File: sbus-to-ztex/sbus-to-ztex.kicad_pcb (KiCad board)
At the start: 4 copper layers, 99.7 x 83.8 mm, 45 parts, among them J1 Conn_01x06_Male, J2 47219-2001, J3 Conn_02x07_Odd_Even, J4 USB_B_Micro, J5 Conn_02x06_Odd_Even, U1 SN74CB3T16211DGGR, U2 SN74CB3T16211DGGR, U3 SN74CB3T16211DGGR, U4 SN74CB3T3125PW, U5 SN65220, U7 TPS2065

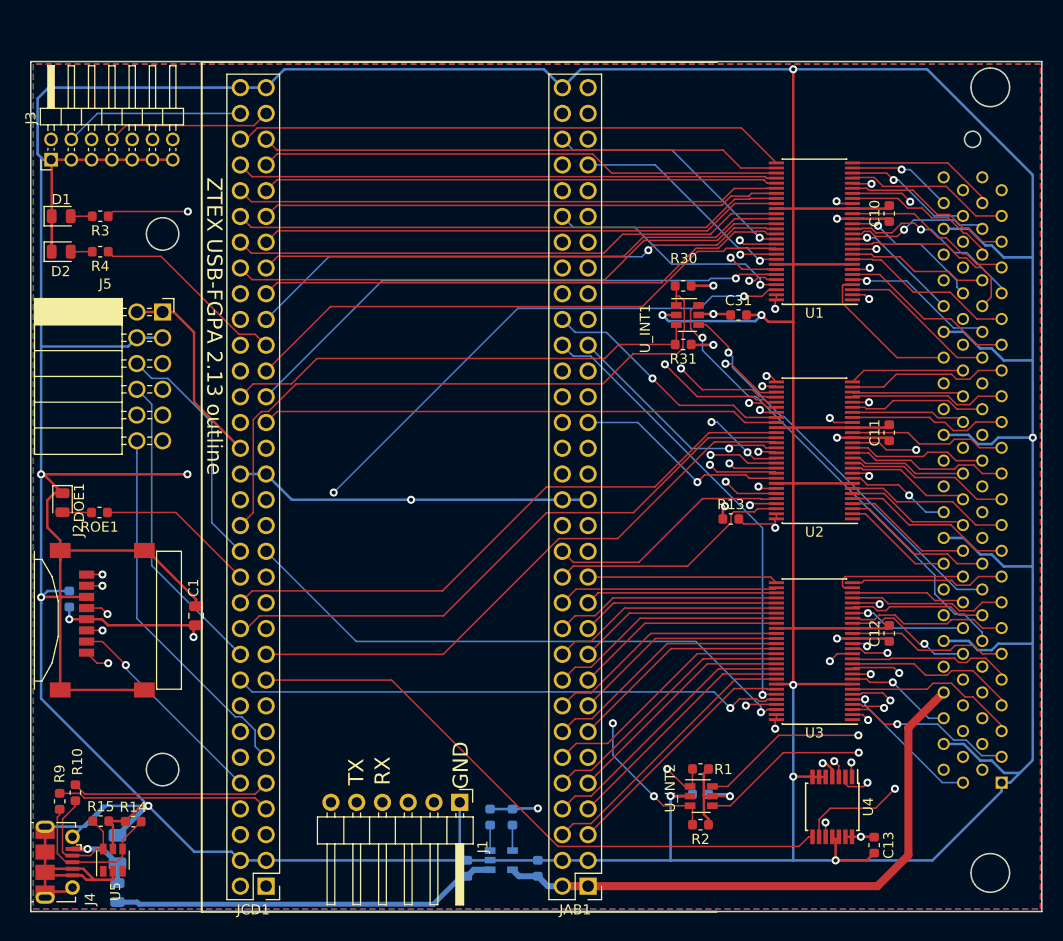
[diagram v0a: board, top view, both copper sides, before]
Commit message: add a pwr header (for e.g. non-pwm fan)
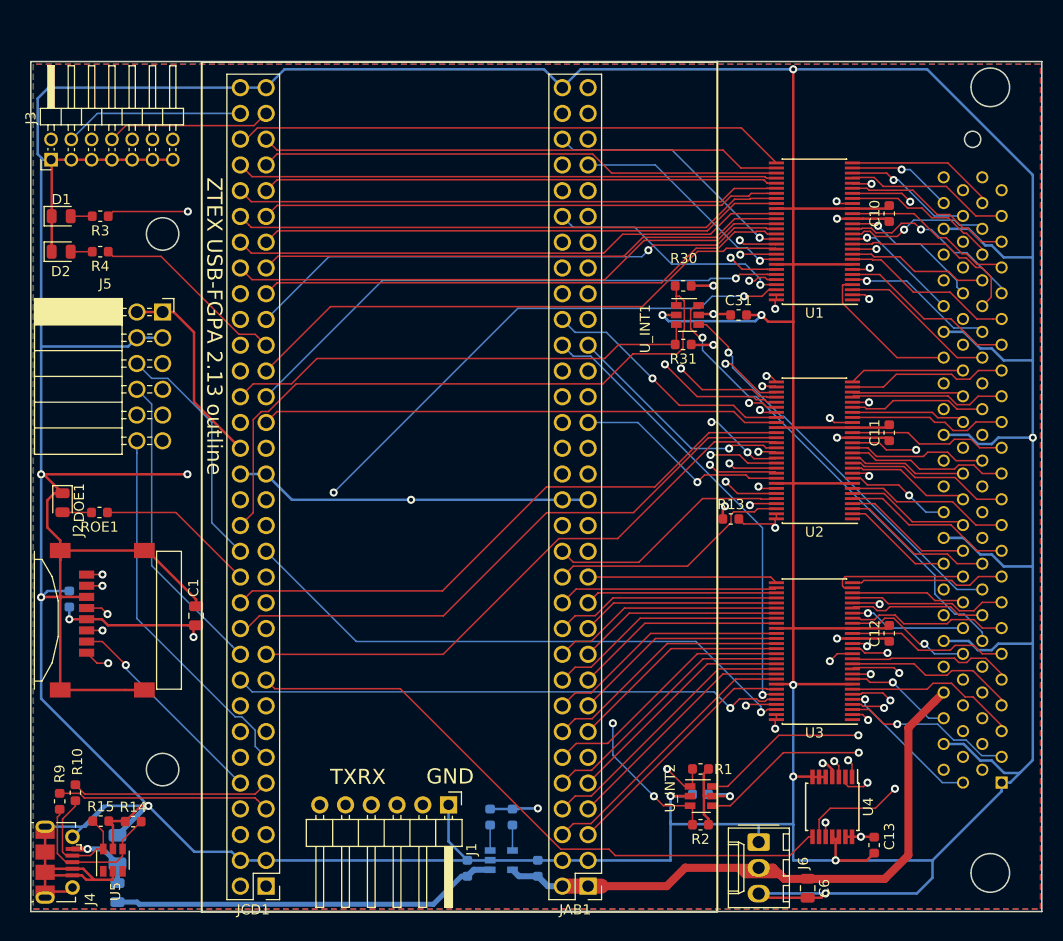
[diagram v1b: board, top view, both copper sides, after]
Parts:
- added C6: 47uF, Capacitor_SMD:C_0805_2012Metric, F.Cu at (173.6, 131.5)
- added J6: Conn_01x03_Male, Connector_Molex:Molex_KK-254_AE-6410-03A_1x03_P2.54mm_Vertical, F.Cu at (168.8, 127.0)
- moved J1 1.13 mm to (138.2, 123.3)
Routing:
- net GND: track 762.6 -> 791.5 mm, vias 13 -> 14
- net +5V: track 103.5 -> 113.2 mm
- net /B2B/TX: track 12.8 -> 11.6 mm
- net /B2B/RX: track 12.8 -> 11.6 mm
- net SBUS_3V3_BG*: track 61.1 -> 61.8 mm

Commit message: more up-to-date
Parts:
- moved R15 2.30 mm to (103.9, 122.6)
- moved C3 2.30 mm to (105.5, 125.4)
- moved R10 2.30 mm to (101.4, 119.8)
- moved R14 2.30 mm to (107.1, 122.7)
- moved R9 2.30 mm to (99.8, 120.7)
- moved U5 2.30 mm to (105.1, 126.5)
- moved FB1 2.30 mm to (105.5, 129.7)
- moved J4 2.30 mm to (99.7, 126.7)
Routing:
- net GND: track 791.5 -> 829.5 mm
- net USBH0_D-: track 19.6 -> 20.6 mm
- net USBH0_D+: track 21.0 -> 21.9 mm
- net /USB/VBus: track 38.2 -> 39.2 mm
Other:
- outline, holes or cut-outs redrawn

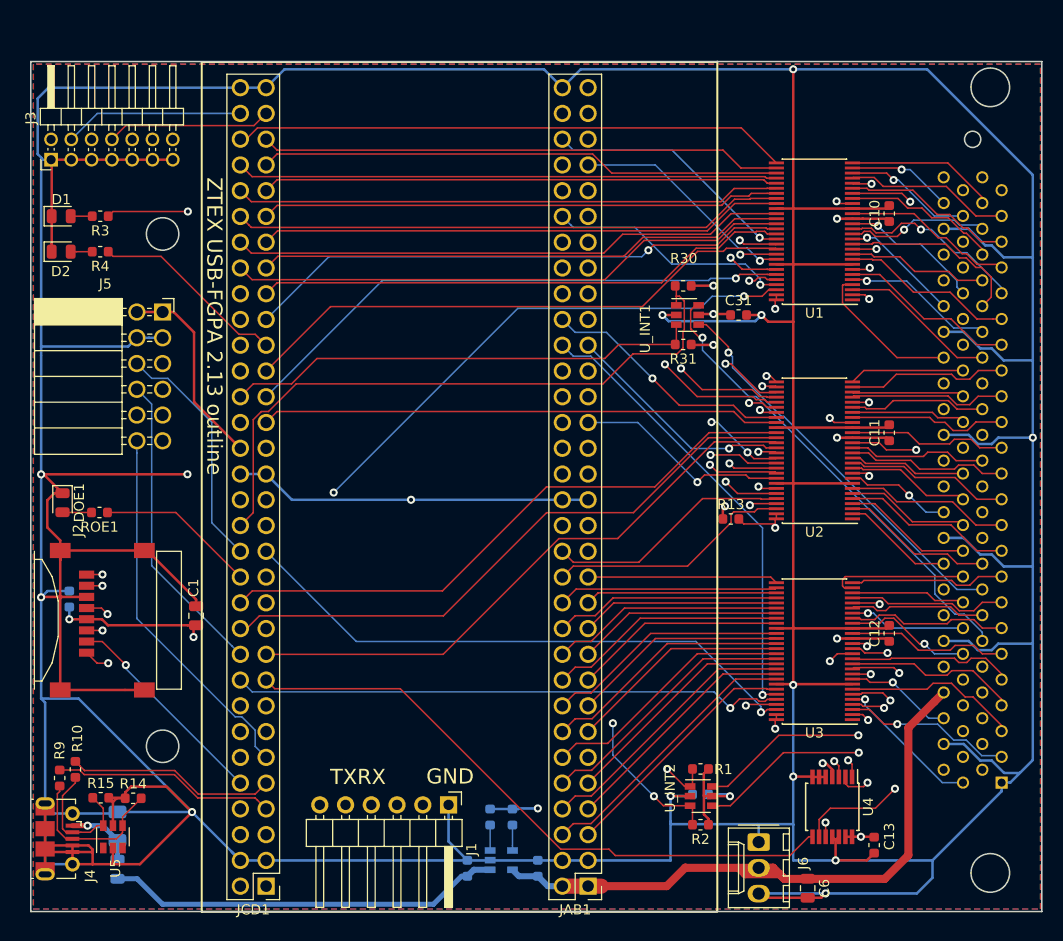
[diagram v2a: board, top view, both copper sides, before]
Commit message: Fewer LEDs, more interrupts, replace USB VBus power chip by something that might be available..., update signals file
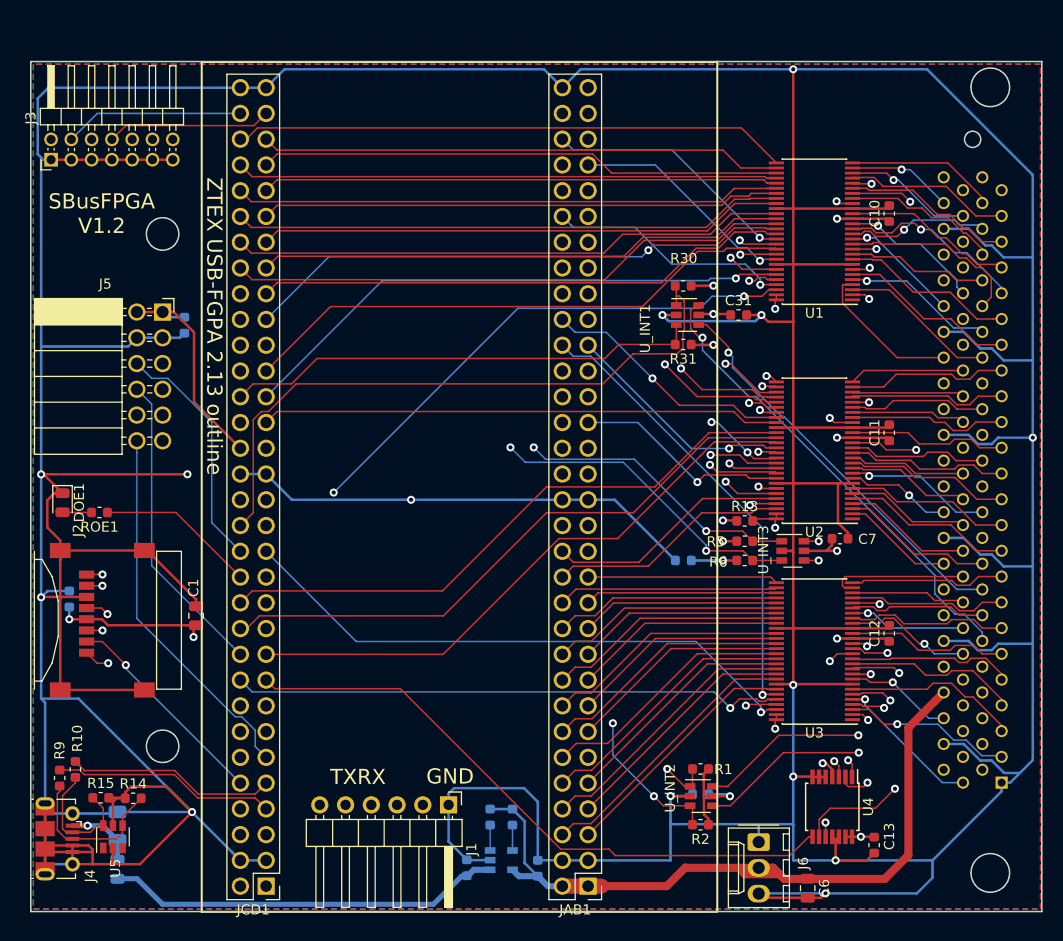
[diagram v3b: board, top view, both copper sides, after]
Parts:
- removed D1, D2: RED, LED_SMD:LED_0805_2012Metric
- removed R20: 1k, Resistor_SMD:R_0603_1608Metric
- removed R3, R4: 549, Resistor_SMD:R_0603_1608Metric
- added C14: 100nF, Capacitor_SMD:C_0603_1608Metric, B.Cu at (140.0, 129.5)
- added C7: 100nF, Capacitor_SMD:C_0603_1608Metric, F.Cu at (176.8, 97.0)
- added C8: 100nF, Capacitor_SMD:C_0603_1608Metric, B.Cu at (161.3, 99.2)
- added C9: 100nF, Capacitor_SMD:C_0603_1608Metric, B.Cu at (112.2, 76.0)
- added R5: 10k, Resistor_SMD:R_0603_1608Metric, F.Cu at (167.4, 97.3)
- added R6: 10k, Resistor_SMD:R_0603_1608Metric, F.Cu at (167.4, 99.2)
- added U_INT3: 74LVC2G07, Package_TO_SOT_SMD:SOT-23-6, F.Cu at (172.2, 98.2)
- C3: value CP -> 150uF
- U7: value TPS2065 -> TPS2051C
- moved R13 1.38 mm to (167.4, 95.3)
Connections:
- J1 pad 2: Net-(J1-Pad2) -> (no net)
- J1 pad 3: Net-(J1-Pad3) -> (no net)
- J1 pad 6: Net-(J1-Pad6) -> (no net)
- J3 pad 12: Net-(J3-Pad12) -> (no net)
- J3 pad 14: Net-(J3-Pad14) -> (no net)
- JAB1 pad 49: LED0 -> SBUS_3V3_INT[6]*
- JCD1 pad 1: Net-(JCD1-Pad1) -> (no net)
- JCD1 pad 2: Net-(JCD1-Pad2) -> (no net)
- JCD1 pad 43: LED1 -> SBUS_3V3_INT[5]*
- R18 pad 2: +3V3 -> +5V
- R19 pad 2: +3V3 -> +5V
- SBus1 pad 28: SBUS_5V_INT[7]* -> (no net)
- SBus1 pad 47: SBUS_5V_DP -> (no net)
- SBus1 pad 48: SBUS_5V_-12V -> (no net)
- SBus1 pad 96: SBUS_5V_+12V -> (no net)
- U1 pad 1: Net-(U1-Pad1) -> (no net)
- U2 pad 1: Net-(U2-Pad1) -> (no net)
- U3 pad 1: Net-(U3-Pad1) -> (no net)
- U5 pad 1: Net-(U5-Pad1) -> (no net)
- U5 pad 3: Net-(U5-Pad3) -> (no net)
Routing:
- net SBUS_3V3_INT[5]*: track 0.00 -> 60.0 mm, vias 0 -> 2
- net SBUS_3V3_INT[6]*: track 0.00 -> 51.6 mm, vias 0 -> 2
- net LED0: track 49.8 -> 0.00 mm, vias 1 -> 0
- net SBUS_5V_INT[6]*: track 0.00 -> 19.8 mm, vias 0 -> 1
- net LED1: track 19.4 -> 0.00 mm
- net SBUS_5V_INT[5]*: track 0.00 -> 18.5 mm, vias 0 -> 1
- net +3V3: track 294.8 -> 283.7 mm, vias 13 -> 15
- net +5V: track 113.2 -> 123.1 mm
- net GND: track 829.5 -> 832.9 mm
- net Net-(D2-Pad2): track 2.12 -> 0.00 mm
- net Net-(D1-Pad2): track 2.12 -> 0.00 mm
- net SBUS_OE: track 121.6 -> 120.2 mm
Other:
- board text added: "SBusFPGA V1.2"

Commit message: Update more stuff to V1.2
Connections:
- J1 pad 2: (no net) -> Net-(J1-Pad2)
- J1 pad 3: (no net) -> Net-(J1-Pad3)
- J1 pad 6: (no net) -> Net-(J1-Pad6)
- J3 pad 12: (no net) -> Net-(J3-Pad12)
- J3 pad 14: (no net) -> Net-(J3-Pad14)
- JAB1 pad 49: SBUS_3V3_INT[6]* -> SBUS_3V3_EER*
- JCD1 pad 1: (no net) -> Net-(JCD1-Pad1)
- JCD1 pad 2: (no net) -> Net-(JCD1-Pad2)
- JCD1 pad 25: SBUS_3V3_EER* -> SBUS_3V3_INT[6]*
- SBus1 pad 28: (no net) -> SBUS_5V_INT[7]*
- SBus1 pad 47: (no net) -> SBUS_5V_DP
- SBus1 pad 48: (no net) -> SBUS_5V_-12V
- SBus1 pad 96: (no net) -> SBUS_5V_+12V
- U1 pad 1: (no net) -> Net-(U1-Pad1)
- U2 pad 1: (no net) -> Net-(U2-Pad1)
- U3 pad 1: (no net) -> Net-(U3-Pad1)
- U5 pad 1: (no net) -> Net-(U5-Pad1)
- U5 pad 3: (no net) -> Net-(U5-Pad3)
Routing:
- net SBUS_3V3_EER*: track 63.0 -> 19.7 mm
- net SBUS_3V3_INT[6]*: track 51.6 -> 53.3 mm, vias 2 -> 1

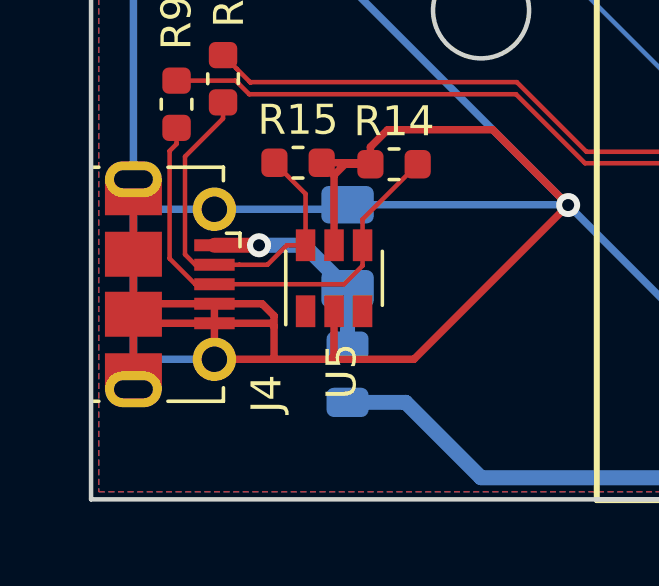
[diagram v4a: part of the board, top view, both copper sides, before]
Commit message: USB ID pin left floating
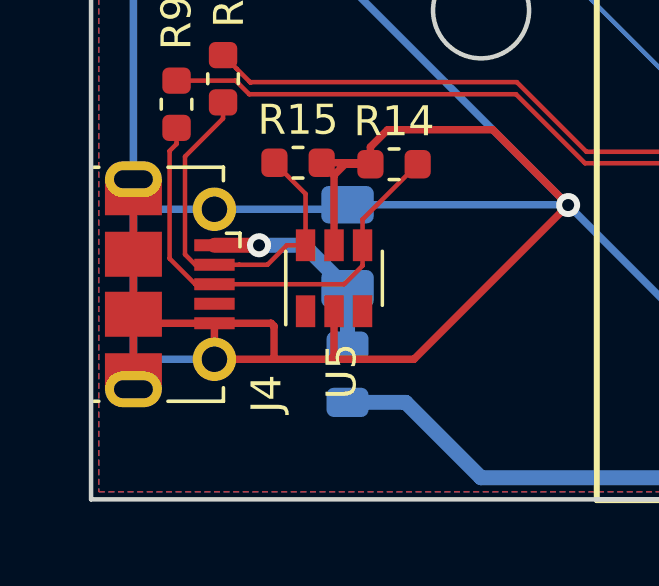
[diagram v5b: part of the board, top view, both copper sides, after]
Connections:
- net Net-(J4-Pad2) renamed /USB/USB_D-
- net Net-(J4-Pad3) renamed /USB/USB_D+
- J1 pad 2: Net-(J1-Pad2) -> (no net)
- J1 pad 3: Net-(J1-Pad3) -> (no net)
- J1 pad 6: Net-(J1-Pad6) -> (no net)
- J3 pad 12: Net-(J3-Pad12) -> (no net)
- J3 pad 14: Net-(J3-Pad14) -> (no net)
- J4 pad 4: GND -> (no net)
- JCD1 pad 1: Net-(JCD1-Pad1) -> (no net)
- JCD1 pad 2: Net-(JCD1-Pad2) -> (no net)
- SBus1 pad 28: SBUS_5V_INT[7]* -> (no net)
- SBus1 pad 47: SBUS_5V_DP -> (no net)
- SBus1 pad 48: SBUS_5V_-12V -> (no net)
- SBus1 pad 96: SBUS_5V_+12V -> (no net)
- U1 pad 1: Net-(U1-Pad1) -> (no net)
- U2 pad 1: Net-(U2-Pad1) -> (no net)
- U3 pad 1: Net-(U3-Pad1) -> (no net)
- U5 pad 1: Net-(U5-Pad1) -> (no net)
- U5 pad 3: Net-(U5-Pad3) -> (no net)
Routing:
- net GND: track 832.9 -> 827.4 mm

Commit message: thinking about a V1.3
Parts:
- removed DOE1: RED, LED_SMD:LED_0805_2012Metric
- removed J1: Conn_01x06_Male, For_SeeedStudio:PinHeader_1x06_P2.54mm_Horizontal_For_SeeedStudio
- removed the J2 at (104.6, 105.1)
- removed J5: Conn_02x06_Odd_Even, For_SeeedStudio:PinSocket_2x06_P2.54mm_Horizontal_For_SeeedStudio
- removed R14, R15: 15k, Resistor_SMD:R_0603_1608Metric
- removed ROE1: 549, Resistor_SMD:R_0603_1608Metric
- removed the U5 at (105.1, 126.5)
- added C15: 100nF 0402, Capacitor_SMD:C_0402_1005Metric, F.Cu at (109.2, 108.0)
- added C16: 10nF 0402, Capacitor_SMD:C_0402_1005Metric, F.Cu at (109.2, 106.5)
- added C17: 47uF 10V 1206, Capacitor_SMD:C_1206_3216Metric, F.Cu at (108.2, 110.5)
- added C18: 100nF 0402, Capacitor_SMD:C_0402_1005Metric, F.Cu at (114.9, 94.5)
- added C19: 100nF 0402, Capacitor_SMD:C_0402_1005Metric, F.Cu at (118.0, 97.3)
- added C20: 100nF 0402, Capacitor_SMD:C_0402_1005Metric, F.Cu at (108.2, 92.0)
- added C21: 10nF 1kV 0805, Capacitor_SMD:C_0805_2012Metric, F.Cu at (100.3, 87.8)
- added C22: 10nF 0402, Capacitor_SMD:C_0402_1005Metric, F.Cu at (134.5, 121.0)
- added C23: 10nF 0402, Capacitor_SMD:C_0402_1005Metric, F.Cu at (164.5, 115.0)
- added C24: 100nF 0402, Capacitor_SMD:C_0402_1005Metric, F.Cu at (149.8, 95.7)
- added C25: 100nF 0402, Capacitor_SMD:C_0402_1005Metric, F.Cu at (109.9, 85.9)
- added C26: 10nF 0402, Capacitor_SMD:C_0402_1005Metric, F.Cu at (112.2, 85.9)
- added C27: 100nF 0402, Capacitor_SMD:C_0402_1005Metric, F.Cu at (172.5, 128.9)
- added H1: MountingHole_Pad, MountingHole:MountingHole_2.2mm_M2_Pad, F.Cu at (100.8, 112.5)
- added J4: 10029449-111RLF (HDMI A), For_SeeedStudio:HDMI_A_Amphenol_10029449-111, F.Cu at (102.2, 99.0)
- added P1: DM3CS-SF, For_SeeedStudio:HRS_DM3CS-SF, F.Cu at (104.5, 75.0)
- added R10: 5.6k, Resistor_SMD:R_0402_1005Metric, F.Cu at (145.5, 121.5)
- added R11: 5.6k, Resistor_SMD:R_0402_1005Metric, F.Cu at (144.0, 119.8)
- added R12: 27, Resistor_SMD:R_0603_1608Metric, F.Cu at (117.5, 83.0)
- added R9: 1M 500V 1206, Resistor_SMD:R_1206_3216Metric, F.Cu at (100.8, 84.8)
- added U10: 74CB3T1G125, Package_TO_SOT_SMD:SOT-23-5, F.Cu at (176.5, 123.5)
- added U6: SRV05-4, Package_TO_SOT_SMD:SOT-23-6, F.Cu at (107.0, 126.3)
- added U7: TPD12S016PWR, For_SeeedStudio:SOP65P640X120-24N, F.Cu at (112.5, 100.7)
- added U8: PCT2075DP, For_SeeedStudio:TSSOP-8_3x3mm_P0.65mm_ForSeeedStudio, F.Cu at (140.0, 120.0)
- added U9: PCT2075DP, For_SeeedStudio:TSSOP-8_3x3mm_P0.65mm_ForSeeedStudio, F.Cu at (165.0, 120.0)
- added X1: ASE-xxxMHz, Oscillator:Oscillator_SMD_Abracon_ASE-4Pin_3.2x2.5mm, F.Cu at (115.6, 86.2)
- C1: value 47uF -> 47uF 10V 1206; footprint Capacitor_SMD:C_0805_2012Metric -> Capacitor_SMD:C_1206_3216Metric
- C10, C11, C12, C13, C31, C7: value 100nF -> 100nF 0402; footprint Capacitor_SMD:C_0603_1608Metric -> Capacitor_SMD:C_0402_1005Metric
- C14, C2, C4, C5, C8: value 100nF -> 100nF 0402; footprint Capacitor_SMD:C_0603_1608Metric -> Capacitor_SMD:C_0402_1005Metric; moved to F.Cu
- C3: value 150uF -> 100uF 1206 (officially 150 uF ? could be >= 100 uF or even less probably); moved to F.Cu
- C6: value 47uF -> 47uF 0805
- C9: value 100nF -> 47uF 0805; footprint Capacitor_SMD:C_0603_1608Metric -> Capacitor_SMD:C_0805_2012Metric; moved to F.Cu
- FB1: moved to F.Cu
- J2: renamed from J4; value USB_B_Micro -> 10118194-0001LF (USB micro-B); footprint Connector_USB:USB_Micro-B_Molex-105017-0001 -> Connector_USB:USB_Micro-B_Amphenol_10118194_Horizontal
- R1, R13, R2, R30, R31, R5, R6: footprint Resistor_SMD:R_0603_1608Metric -> Resistor_SMD:R_0402_1005Metric
- R7: renamed from R18; footprint Resistor_SMD:R_0603_1608Metric -> Resistor_SMD:R_0402_1005Metric; moved to F.Cu
- R8: renamed from R19; footprint Resistor_SMD:R_0603_1608Metric -> Resistor_SMD:R_0402_1005Metric; moved to F.Cu
- U4: value SN74CB3T3125PW -> 74CB3T1G125; footprint Package_SO:TSSOP-14_4.4x5mm_P0.65mm -> Package_TO_SOT_SMD:SOT-23-5
- U5: renamed from U7; value TPS2051C -> TPS2051CDBV; moved to F.Cu
- U_INT1, U_INT2, U_INT3: footprint Package_TO_SOT_SMD:SOT-23-6 -> For_SeeedStudio:SOT65P210X110-6N
- moved J6 76.1 mm to (182.0, 52.0)
- moved C9 67.8 mm to (176.8, 55.5)
- moved C1 40.6 mm to (106.0, 64.8)
- moved C2 37.3 mm to (102.0, 65.8)
- moved C8 34.4 mm to (127.5, 93.2), turned to 0 degrees
- moved J3 33.8 mm to (132.5, 55.2)
- moved FB1 30.5 mm to (136.0, 130.6), turned to 180 degrees
- moved R13 28.1 mm to (179.2, 120.8), turned to 180 degrees
- moved U_INT1 27.3 mm to (176.5, 98.0)
- moved R30 27.3 mm to (173.5, 96.5), turned to 270 degrees
- moved C31 26.8 mm to (180.5, 98.0)
- moved R31 24.8 mm to (173.5, 99.5), turned to 90 degrees
- moved R5 21.6 mm to (173.5, 76.5), turned to 270 degrees
- moved U_INT3 20.7 mm to (176.5, 78.0)
- moved R6 20.7 mm to (173.5, 79.5), turned to 90 degrees
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- renumbered R9 to R3, R10 to R4
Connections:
- C9 pad 1: +3V3 -> +5V
- J2 pad 6: GND -> SHIELD
- JAB1 pad 10: SBUS_3V3_D[04] -> SBUS_OE
- JAB1 pad 11: SBUS_3V3_INT[2]* -> SBUS_3V3_AS*
- JAB1 pad 12: SBUS_3V3_D[06] -> SBUS_3V3_SEL*
- JAB1 pad 13: SBUS_3V3_D[07] -> SBUS_3V3_D[01]
- JAB1 pad 14: SBUS_3V3_D[08] -> SBUS_3V3_D[02]
- JAB1 pad 15: SBUS_3V3_D[09] -> SBUS_3V3_D[04]
- JAB1 pad 16: SBUS_3V3_D[10] -> SBUS_3V3_D[05]
- JAB1 pad 17: SBUS_3V3_D[11] -> SBUS_3V3_D[07]
- JAB1 pad 18: SBUS_3V3_D[12] -> SBUS_3V3_D[08]
- JAB1 pad 19: SBUS_3V3_D[13] -> SBUS_3V3_D[10]
- JAB1 pad 20: SBUS_3V3_D[14] -> SBUS_3V3_CLK
- JAB1 pad 21: SBUS_3V3_D[15] -> SBUS_3V3_D[12]
- JAB1 pad 22: SBUS_3V3_D[16] -> SBUS_3V3_D[13]
- JAB1 pad 23: SBUS_3V3_D[17] -> SBUS_3V3_D[15]
- JAB1 pad 24: SBUS_3V3_D[18] -> SBUS_3V3_D[16]
- JAB1 pad 25: SBUS_3V3_D[19] -> SBUS_3V3_D[18]
- JAB1 pad 26: SBUS_3V3_D[20] -> SBUS_3V3_D[19]
- JAB1 pad 35: SBUS_3V3_D[23] -> SBUS_3V3_D[30]
- JAB1 pad 36: SBUS_3V3_D[24] -> SBUS_3V3_D[31]
- JAB1 pad 37: SBUS_3V3_D[25] -> SBUS_3V3_SIZ[0]
- JAB1 pad 38: SBUS_3V3_D[26] -> SBUS_3V3_PPRD
- JAB1 pad 39: SBUS_3V3_D[27] -> SBUS_3V3_PA[01]
- JAB1 pad 40: SBUS_3V3_D[28] -> SBUS_3V3_PA[00]
- JAB1 pad 41: SBUS_3V3_D[29] -> SBUS_3V3_PA[02]
- JAB1 pad 42: SBUS_3V3_D[30] -> SBUS_3V3_PA[05]
- JAB1 pad 43: SBUS_3V3_D[31] -> SBUS_3V3_EER*
- JAB1 pad 44: SBUS_3V3_CLK -> SBUS_3V3_PA[07]
- JAB1 pad 45: SBUS_3V3_PA[01] -> SBUS_3V3_PA[09]
- JAB1 pad 46: SBUS_3V3_PA[00] -> SBUS_3V3_PA[08]
- JAB1 pad 47: SBUS_3V3_PA[03] -> SBUS_3V3_PA[10]
- JAB1 pad 48: SBUS_3V3_PA[02] -> SBUS_3V3_ACK[0]*
- JAB1 pad 49: SBUS_3V3_EER* -> SBUS_3V3_PA[12]
- JAB1 pad 5: SBUS_3V3_D[01] -> SBUS_3V3_BR*
- JAB1 pad 50: SBUS_3V3_PA[04] -> SBUS_3V3_PA[15]
- JAB1 pad 51: SBUS_3V3_PA[05] -> SBUS_3V3_PA[17]
- JAB1 pad 52: SBUS_3V3_PA[06] -> SBUS_3V3_PA[16]
- JAB1 pad 53: SBUS_3V3_PA[07] -> SBUS_3V3_PA[19]
- JAB1 pad 54: SBUS_3V3_PA[08] -> SBUS_3V3_PA[18]
- JAB1 pad 55: SBUS_3V3_PA[09] -> SBUS_3V3_PA[20]
- JAB1 pad 56: SBUS_3V3_PA[10] -> SBUS_3V3_PA[23]
- JAB1 pad 57: SBUS_3V3_PA[11] -> SBUS_3V3_ACK[2]*
- JAB1 pad 58: SBUS_3V3_PA[12] -> SBUS_3V3_PA[25]
- JAB1 pad 59: SBUS_3V3_PA[13] -> SBUS_3V3_PA[27]
- JAB1 pad 6: SBUS_3V3_D[00] -> I2C0_SDA
- JAB1 pad 60: SBUS_3V3_PA[14] -> SBUS_3V3_PA[26]
- JAB1 pad 7: SBUS_3V3_D[03] -> SBUS_3V3_BG*
- JAB1 pad 8: SBUS_3V3_D[02] -> I2C0_SCL
- JAB1 pad 9: SBUS_3V3_D[05] -> SBUS_3V3_INT[1]*
- JCD1 pad 10: SD_D3 -> HDMI_D2-
- JCD1 pad 11: PMOD-12 -> SBUS_3V3_INT[4]*
- JCD1 pad 12: SD_D0 -> HDMI_D1+
- JCD1 pad 13: PMOD-11 -> SBUS_3V3_INT[5]*
- JCD1 pad 14: SD_D1 -> HDMI_D1-
- JCD1 pad 15: SD_CLK -> SBUS_3V3_INT[6]*
- JCD1 pad 16: SD_CMD -> HDMI_D0+
- JCD1 pad 17: SBUS_3V3_BG* -> SBUS_3V3_D[00]
- JCD1 pad 18: SBUS_3V3_AS* -> HDMI_D0-
- JCD1 pad 19: SBUS_3V3_SIZ[0] -> SBUS_3V3_D[03]
- JCD1 pad 20: PMOD-8 -> HDMI_CLK+
- JCD1 pad 21: SBUS_3V3_BR* -> SBUS_3V3_D[06]
- JCD1 pad 22: SBUS_3V3_SIZ[1] -> HDMI_CLK-
- JCD1 pad 23: SBUS_3V3_INT[1]* -> SBUS_3V3_D[09]
- JCD1 pad 24: SBUS_3V3_SIZ[2] -> SBUS_3V3_D[11]
- JCD1 pad 25: SBUS_3V3_INT[6]* -> SBUS_3V3_D[14]
- JCD1 pad 26: SBUS_DATA_OE_LED -> SBUS_3V3_D[17]
- JCD1 pad 27: SBUS_3V3_RST* -> SBUS_3V3_D[20]
- JCD1 pad 28: PMOD-6 -> SBUS_3V3_D[23]
- JCD1 pad 29: SBUS_3V3_SEL* -> SBUS_3V3_D[24]
- JCD1 pad 30: SBUS_3V3_INT[3]* -> SBUS_3V3_D[25]
- JCD1 pad 37: SBUS_3V3_PPRD -> SBUS_3V3_D[27]
- JCD1 pad 38: SBUS_OE -> SBUS_3V3_D[26]
- JCD1 pad 39: SBUS_3V3_ACK[0]* -> SBUS_3V3_D[28]
- JCD1 pad 40: SBUS_3V3_INT[4]* -> CLK_54_000
- JCD1 pad 41: SBUS_3V3_ACK[1]* -> SBUS_3V3_D[29]
- JCD1 pad 42: PMOD-10 -> SD_D2
- JCD1 pad 43: SBUS_3V3_INT[5]* -> SBUS_3V3_SIZ[1]
- JCD1 pad 44: PMOD-9 -> SD_D3
- JCD1 pad 45: SBUS_3V3_ACK[2]* -> SBUS_3V3_SIZ[2]
- JCD1 pad 46: PMOD-7 -> SD_CMD
- JCD1 pad 47: SBUS_3V3_PA[15] -> SBUS_3V3_PA[03]
- JCD1 pad 48: PMOD-5 -> SD_CLK
- JCD1 pad 49: SBUS_3V3_PA[17] -> SBUS_3V3_PA[04]
- JCD1 pad 5: /B2B/RX -> USBH0_D+
- JCD1 pad 50: SBUS_3V3_PA[16] -> SD_D0
- JCD1 pad 51: SBUS_3V3_PA[19] -> SBUS_3V3_PA[06]
- JCD1 pad 52: SBUS_3V3_PA[18] -> SD_D1
- JCD1 pad 53: SBUS_3V3_PA[21] -> SBUS_3V3_PA[11]
- JCD1 pad 54: SBUS_3V3_PA[20] -> SBUS_3V3_PA[13]
- JCD1 pad 55: SBUS_3V3_PA[23] -> SBUS_3V3_PA[14]
- JCD1 pad 56: SBUS_3V3_PA[22] -> SBUS_3V3_ACK[1]*
- JCD1 pad 57: SBUS_3V3_PA[25] -> SBUS_3V3_PA[21]
- JCD1 pad 58: SBUS_3V3_PA[24] -> SBUS_3V3_PA[22]
- JCD1 pad 59: SBUS_3V3_PA[27] -> SBUS_3V3_PA[24]
- JCD1 pad 6: /B2B/TX -> USBH0_D-
- JCD1 pad 60: SBUS_3V3_PA[26] -> SBUS_3V3_RST*
- JCD1 pad 7: USBH0_D+ -> SBUS_3V3_INT[2]*
- JCD1 pad 8: SD_D2 -> HDMI_D2+
- JCD1 pad 9: USBH0_D- -> SBUS_3V3_INT[3]*
- R30 pad 2: SBUS_3V3_INT[3]* -> SBUS_3V3_INT[4]*
- R31 pad 2: SBUS_3V3_INT[4]* -> SBUS_3V3_INT[3]*
- U1 pad 10: SBUS_5V_ACK[1]* -> SBUS_3V3_PA[23]
- U1 pad 11: SBUS_5V_PA[13] -> SBUS_3V3_PA[20]
- U1 pad 12: SBUS_5V_PA[14] -> SBUS_3V3_PA[21]
- U1 pad 13: SBUS_5V_PA[15] -> SBUS_3V3_PA[18]
- U1 pad 14: SBUS_5V_ACK[2]* -> SBUS_3V3_PA[19]
- U1 pad 15: SBUS_5V_PA[16] -> SBUS_3V3_ACK[1]*
- U1 pad 16: SBUS_5V_PA[17] -> SBUS_3V3_PA[16]
- U1 pad 18: SBUS_5V_PA[18] -> SBUS_3V3_PA[17]
- U1 pad 2: SBUS_5V_EER* -> SBUS_3V3_RST*
- U1 pad 20: SBUS_5V_PA[19] -> SBUS_3V3_PA[14]
- U1 pad 21: SBUS_5V_PA[20] -> SBUS_3V3_PA[15]
- U1 pad 22: SBUS_5V_PA[21] -> SBUS_3V3_PA[12]
- U1 pad 23: SBUS_5V_PA[22] -> SBUS_3V3_PA[13]
- U1 pad 24: SBUS_5V_PA[23] -> SBUS_3V3_ACK[0]*
- U1 pad 25: SBUS_5V_PA[24] -> SBUS_3V3_PA[10]
- U1 pad 26: SBUS_5V_PA[25] -> SBUS_3V3_PA[11]
- U1 pad 27: SBUS_5V_PA[27] -> SBUS_3V3_PA[08]
- U1 pad 28: SBUS_5V_PA[26] -> SBUS_3V3_PA[09]
- U1 pad 29: SBUS_3V3_PA[26] -> SBUS_5V_PA[09]
- U1 pad 3: SBUS_5V_PA[08] -> SBUS_3V3_PA[26]
- U1 pad 30: SBUS_3V3_PA[27] -> SBUS_5V_PA[08]
- U1 pad 31: SBUS_3V3_PA[25] -> SBUS_5V_PA[11]
- U1 pad 32: SBUS_3V3_PA[24] -> SBUS_5V_PA[10]
- U1 pad 33: SBUS_3V3_PA[23] -> SBUS_5V_ACK[0]*
- U1 pad 34: SBUS_3V3_PA[22] -> SBUS_5V_PA[13]
- U1 pad 35: SBUS_3V3_PA[21] -> SBUS_5V_PA[12]
- U1 pad 36: SBUS_3V3_PA[20] -> SBUS_5V_PA[15]
- U1 pad 37: SBUS_3V3_PA[19] -> SBUS_5V_PA[14]
- U1 pad 39: SBUS_3V3_PA[18] -> SBUS_5V_PA[17]
- U1 pad 4: SBUS_5V_PA[09] -> SBUS_3V3_PA[27]
- U1 pad 40: SBUS_3V3_PA[17] -> SBUS_5V_PA[16]
- U1 pad 41: SBUS_3V3_PA[16] -> SBUS_5V_ACK[1]*
- U1 pad 42: SBUS_3V3_ACK[2]* -> SBUS_5V_PA[19]
- U1 pad 43: SBUS_3V3_PA[15] -> SBUS_5V_PA[18]
- U1 pad 44: SBUS_3V3_PA[14] -> SBUS_5V_PA[21]
- U1 pad 45: SBUS_3V3_PA[13] -> SBUS_5V_PA[20]
- U1 pad 46: SBUS_3V3_ACK[1]* -> SBUS_5V_PA[23]
- U1 pad 47: SBUS_3V3_PA[12] -> SBUS_5V_PA[22]
- U1 pad 48: SBUS_3V3_PA[11] -> SBUS_5V_ACK[2]*
- U1 pad 5: SBUS_5V_ACK[0]* -> SBUS_3V3_PA[24]
- U1 pad 50: SBUS_3V3_PA[10] -> SBUS_5V_PA[25]
- U1 pad 51: SBUS_3V3_ACK[0]* -> SBUS_5V_PA[24]
- U1 pad 52: SBUS_3V3_PA[09] -> SBUS_5V_PA[27]
- U1 pad 53: SBUS_3V3_PA[08] -> SBUS_5V_PA[26]
- U1 pad 54: SBUS_3V3_EER* -> SBUS_5V_RST*
- U1 pad 6: SBUS_5V_PA[10] -> SBUS_3V3_PA[25]
- U1 pad 7: SBUS_5V_PA[11] -> SBUS_3V3_ACK[2]*
- U1 pad 9: SBUS_5V_PA[12] -> SBUS_3V3_PA[22]
- U2 pad 10: SBUS_5V_D[27] -> SBUS_3V3_PA[00]
- U2 pad 11: SBUS_5V_D[28] -> SBUS_3V3_PA[01]
- U2 pad 12: SBUS_5V_D[29] -> SBUS_3V3_SIZ[2]
- U2 pad 13: SBUS_5V_D[30] -> SBUS_3V3_PPRD
- U2 pad 14: SBUS_5V_D[31] -> SBUS_3V3_SIZ[0]
- U2 pad 15: SBUS_5V_SIZ[0] -> SBUS_3V3_SIZ[1]
- U2 pad 16: SBUS_5V_SIZ[1] -> SBUS_3V3_D[31]
- U2 pad 18: SBUS_5V_SIZ[2] -> SBUS_3V3_D[30]
- U2 pad 2: SBUS_5V_D[20] -> SBUS_3V3_PA[06]
- U2 pad 20: SBUS_5V_PPRD -> SBUS_3V3_D[29]
- U2 pad 21: SBUS_5V_PA[00] -> SBUS_3V3_D[28]
- U2 pad 22: SBUS_5V_PA[01] -> SBUS_3V3_D[27]
- U2 pad 23: SBUS_5V_PA[02] -> SBUS_3V3_D[26]
- U2 pad 24: SBUS_5V_PA[03] -> SBUS_3V3_D[25]
- U2 pad 25: SBUS_5V_PA[04] -> SBUS_3V3_D[24]
- U2 pad 26: SBUS_5V_PA[05] -> SBUS_3V3_D[23]
- U2 pad 27: SBUS_5V_PA[06] -> SBUS_3V3_D[22]
- U2 pad 28: SBUS_5V_PA[07] -> SBUS_3V3_D[21]
- U2 pad 29: SBUS_3V3_PA[07] -> SBUS_5V_D[21]
- U2 pad 3: SBUS_5V_D[21] -> SBUS_3V3_PA[07]
- U2 pad 30: SBUS_3V3_PA[06] -> SBUS_5V_D[22]
- U2 pad 31: SBUS_3V3_PA[05] -> SBUS_5V_D[23]
- U2 pad 32: SBUS_3V3_PA[04] -> SBUS_5V_D[24]
- U2 pad 33: SBUS_3V3_PA[03] -> SBUS_5V_D[25]
- U2 pad 34: SBUS_3V3_PA[02] -> SBUS_5V_D[26]
- U2 pad 35: SBUS_3V3_PA[01] -> SBUS_5V_D[27]
- U2 pad 36: SBUS_3V3_PA[00] -> SBUS_5V_D[28]
- U2 pad 37: SBUS_3V3_PPRD -> SBUS_5V_D[29]
- U2 pad 39: SBUS_3V3_SIZ[2] -> SBUS_5V_D[30]
- U2 pad 4: SBUS_5V_D[22] -> SBUS_3V3_EER*
- U2 pad 40: SBUS_3V3_SIZ[1] -> SBUS_5V_D[31]
- U2 pad 41: SBUS_3V3_SIZ[0] -> SBUS_5V_SIZ[1]
- U2 pad 42: SBUS_3V3_D[31] -> SBUS_5V_SIZ[0]
- U2 pad 43: SBUS_3V3_D[30] -> SBUS_5V_PPRD
- U2 pad 44: SBUS_3V3_D[29] -> SBUS_5V_SIZ[2]
- U2 pad 45: SBUS_3V3_D[28] -> SBUS_5V_PA[01]
- U2 pad 46: SBUS_3V3_D[27] -> SBUS_5V_PA[00]
- U2 pad 47: SBUS_3V3_D[26] -> SBUS_5V_PA[03]
- U2 pad 48: SBUS_3V3_D[25] -> SBUS_5V_PA[02]
- U2 pad 5: SBUS_5V_D[23] -> SBUS_3V3_PA[04]
- U2 pad 50: SBUS_3V3_D[24] -> SBUS_5V_PA[05]
- U2 pad 51: SBUS_3V3_D[23] -> SBUS_5V_PA[04]
- U2 pad 52: SBUS_3V3_D[22] -> SBUS_5V_EER*
- U2 pad 53: SBUS_3V3_D[21] -> SBUS_5V_PA[07]
- U2 pad 54: SBUS_3V3_D[20] -> SBUS_5V_PA[06]
- U2 pad 6: SBUS_5V_D[24] -> SBUS_3V3_PA[05]
- U2 pad 7: SBUS_5V_D[25] -> SBUS_3V3_PA[02]
- U2 pad 9: SBUS_5V_D[26] -> SBUS_3V3_PA[03]
- U3 pad 10: SBUS_5V_D[02] -> SBUS_3V3_D[13]
- U3 pad 11: SBUS_5V_D[05] -> SBUS_3V3_D[12]
- U3 pad 12: SBUS_5V_D[04] -> SBUS_3V3_D[11]
- U3 pad 13: SBUS_5V_D[06] -> SBUS_3V3_D[10]
- U3 pad 14: SBUS_5V_D[07] -> SBUS_3V3_D[09]
- U3 pad 15: SBUS_5V_D[08] -> SBUS_3V3_D[08]
- U3 pad 16: SBUS_5V_D[09] -> SBUS_3V3_D[07]
- U3 pad 18: SBUS_5V_D[10] -> SBUS_3V3_D[06]
- U3 pad 2: SBUS_5V_RST* -> SBUS_3V3_D[20]
- U3 pad 20: SBUS_5V_D[11] -> SBUS_3V3_D[05]
- U3 pad 21: SBUS_5V_D[12] -> SBUS_3V3_D[04]
- U3 pad 22: SBUS_5V_D[13] -> SBUS_3V3_D[03]
- U3 pad 23: SBUS_5V_D[14] -> SBUS_3V3_D[02]
- U3 pad 24: SBUS_5V_D[15] -> SBUS_3V3_D[01]
- U3 pad 25: SBUS_5V_D[16] -> SBUS_3V3_D[00]
- U3 pad 26: SBUS_5V_D[17] -> SBUS_3V3_SEL*
- U3 pad 27: SBUS_5V_D[18] -> SBUS_3V3_AS*
- U3 pad 28: SBUS_5V_D[19] -> SBUS_3V3_CLK
- U3 pad 29: SBUS_3V3_D[19] -> SBUS_5V_CLK
- U3 pad 3: SBUS_5V_SEL* -> SBUS_3V3_D[19]
- U3 pad 30: SBUS_3V3_D[18] -> SBUS_5V_AS*
- U3 pad 31: SBUS_3V3_D[17] -> SBUS_5V_SEL*
- U3 pad 32: SBUS_3V3_D[16] -> SBUS_5V_D[00]
- U3 pad 33: SBUS_3V3_D[15] -> SBUS_5V_D[01]
- U3 pad 34: SBUS_3V3_D[14] -> SBUS_5V_D[02]
- U3 pad 35: SBUS_3V3_D[13] -> SBUS_5V_D[03]
- U3 pad 36: SBUS_3V3_D[12] -> SBUS_5V_D[04]
- U3 pad 37: SBUS_3V3_D[11] -> SBUS_5V_D[05]
- U3 pad 39: SBUS_3V3_D[10] -> SBUS_5V_D[06]
- U3 pad 4: SBUS_5V_AS* -> SBUS_3V3_D[18]
- U3 pad 40: SBUS_3V3_D[09] -> SBUS_5V_D[07]
- U3 pad 41: SBUS_3V3_D[08] -> SBUS_5V_D[08]
- U3 pad 42: SBUS_3V3_D[07] -> SBUS_5V_D[09]
- U3 pad 43: SBUS_3V3_D[06] -> SBUS_5V_D[10]
- U3 pad 44: SBUS_3V3_D[04] -> SBUS_5V_D[11]
- U3 pad 45: SBUS_3V3_D[05] -> SBUS_5V_D[12]
- U3 pad 46: SBUS_3V3_D[02] -> SBUS_5V_D[13]
- U3 pad 47: SBUS_3V3_D[03] -> SBUS_5V_D[14]
- U3 pad 48: SBUS_3V3_D[00] -> SBUS_5V_D[15]
- U3 pad 5: SBUS_5V_CLK -> SBUS_3V3_D[17]
- U3 pad 50: SBUS_3V3_D[01] -> SBUS_5V_D[16]
- U3 pad 51: SBUS_3V3_CLK -> SBUS_5V_D[17]
- U3 pad 52: SBUS_3V3_AS* -> SBUS_5V_D[18]
- U3 pad 53: SBUS_3V3_SEL* -> SBUS_5V_D[19]
- U3 pad 54: SBUS_3V3_RST* -> SBUS_5V_D[20]
- U3 pad 6: SBUS_5V_D[01] -> SBUS_3V3_D[16]
- U3 pad 7: SBUS_5V_D[00] -> SBUS_3V3_D[15]
- U3 pad 9: SBUS_5V_D[03] -> SBUS_3V3_D[14]
- U4 pad 3: SBUS_3V3_BR* -> GND
- U4 pad 4: +3V3 -> SBUS_3V3_BR*
- U4 pad 5: GND -> +3V3
- U_INT1 pad 1: SBUS_3V3_INT[3]* -> SBUS_3V3_INT[4]*
- U_INT1 pad 3: SBUS_3V3_INT[4]* -> SBUS_3V3_INT[3]*
- U_INT1 pad 4: SBUS_5V_INT[4]* -> SBUS_5V_INT[3]*
- U_INT1 pad 6: SBUS_5V_INT[3]* -> SBUS_5V_INT[4]*
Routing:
- net GND: track 827.4 -> 105.4 mm, vias 14 -> 52
- net +3V3: track 283.7 -> 80.6 mm, vias 15 -> 25
- net SHIELD: track 0.00 -> 62.2 mm
- net SBUS_5V_RST*: track 57.9 -> 10.4 mm, vias 1 -> 0
- net SBUS_3V3_BR*: track 63.2 -> 20.0 mm, vias 1 -> 0
- net SBUS_3V3_SIZ[0]: track 59.0 -> 16.4 mm
- net SBUS_3V3_INT[2]*: track 13.2 -> 55.2 mm
- net SBUS_3V3_BG*: track 61.8 -> 20.1 mm
- net SBUS_3V3_SEL*: track 57.7 -> 20.0 mm, vias 1 -> 0
- net SBUS_3V3_PA[20]: track 54.5 -> 17.0 mm
- net SBUS_3V3_AS*: track 54.6 -> 17.3 mm, vias 1 -> 0
- net SBUS_3V3_ACK[2]*: track 54.1 -> 17.2 mm, vias 1 -> 0
- net PMOD-12: track 36.9 -> 0.00 mm
- net SBUS_3V3_ACK[0]*: track 55.4 -> 18.9 mm, vias 1 -> 0
- net SBUS_3V3_PA[16]: track 55.6 -> 19.3 mm
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- added copper zone on In2.Cu, net +5V
- added copper zone on In1.Cu, net GND
- removed copper zone on In1.Cu, net +3V3
- removed copper zone on In1.Cu, net /USB/VBus_USB0
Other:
- outline, holes or cut-outs redrawn
- net class Default: via_dia 0.8 -> 0.45; via_drill 0.4 -> 0.3
- board text added: "1"
- board text added: "JTAG"
- board text added: "SBusFPGA V1.3"
- board text added: "ZTex 2.13 outline"
- board text removed: "GND"
- board text removed: "RX"
- board text removed: "SBusFPGA V1.2"
- board text removed: "TX"
- board text removed: "ZTEX USB-FGPA 2.13 outline"
